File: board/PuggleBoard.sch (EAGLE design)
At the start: 130 parts, among them U1 LMP7704, U10 SN65LVDS2, U11 SN65LVDS1, U12 SN65LVDS1, U13 SN65LVDS1, U14 SN65MLVD201D, U15 24C, U2 ADS8331, U3 OPA4209, U4 AD5686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

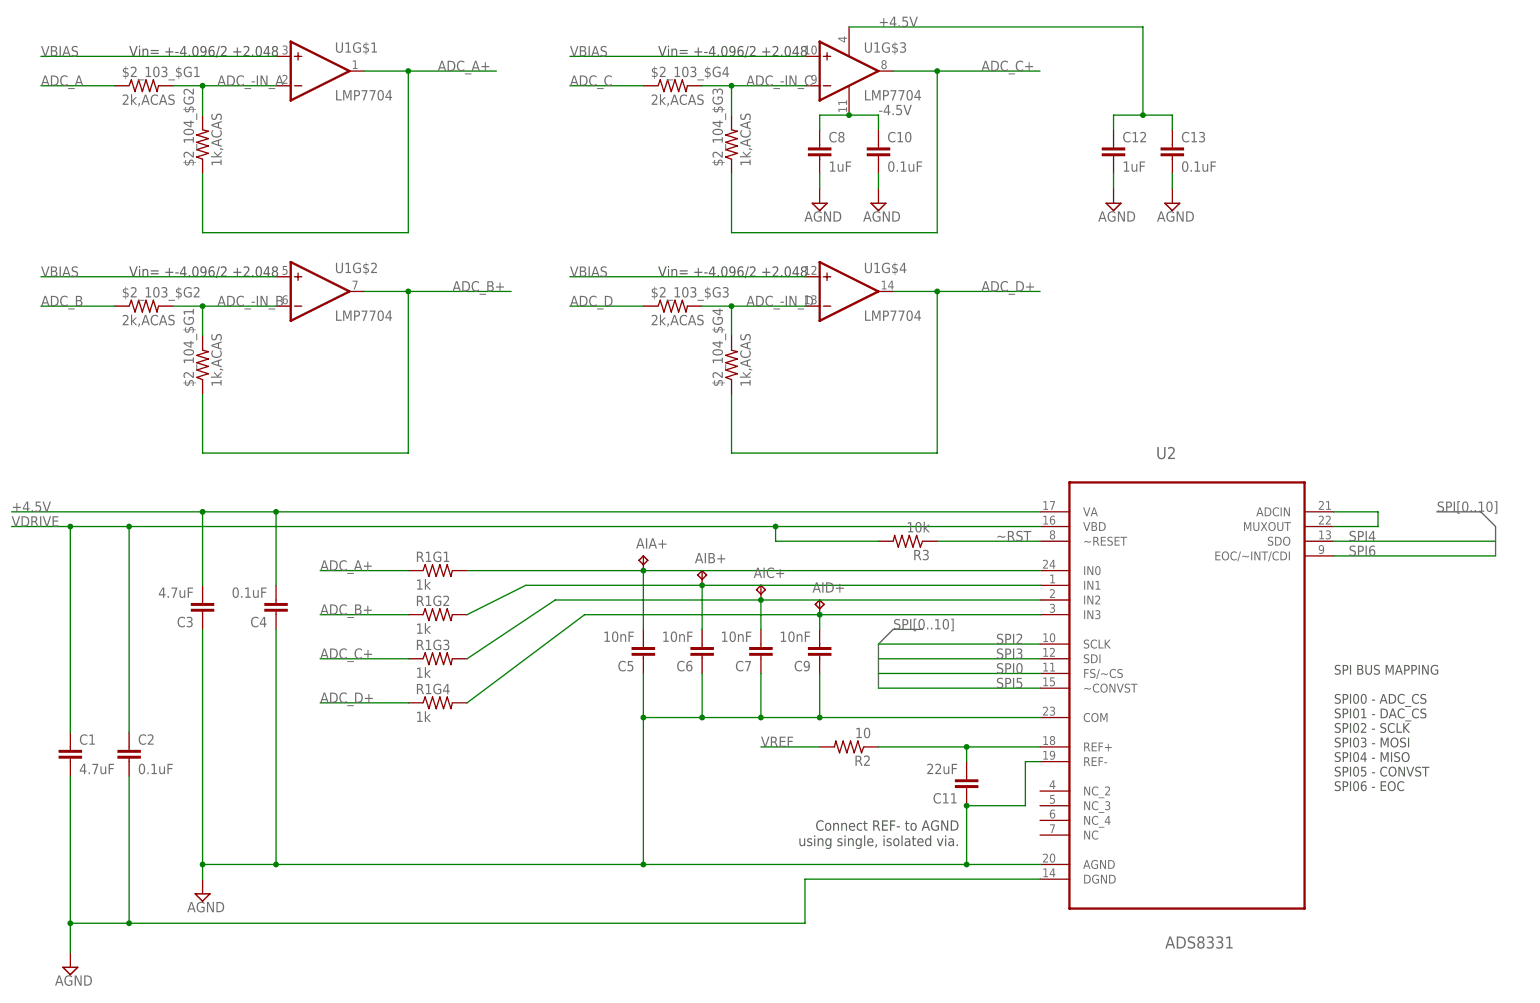
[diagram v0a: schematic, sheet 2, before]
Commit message: Nearly finished with layout. Need to get digital planes and LVDS signals routed. Hard parts done.
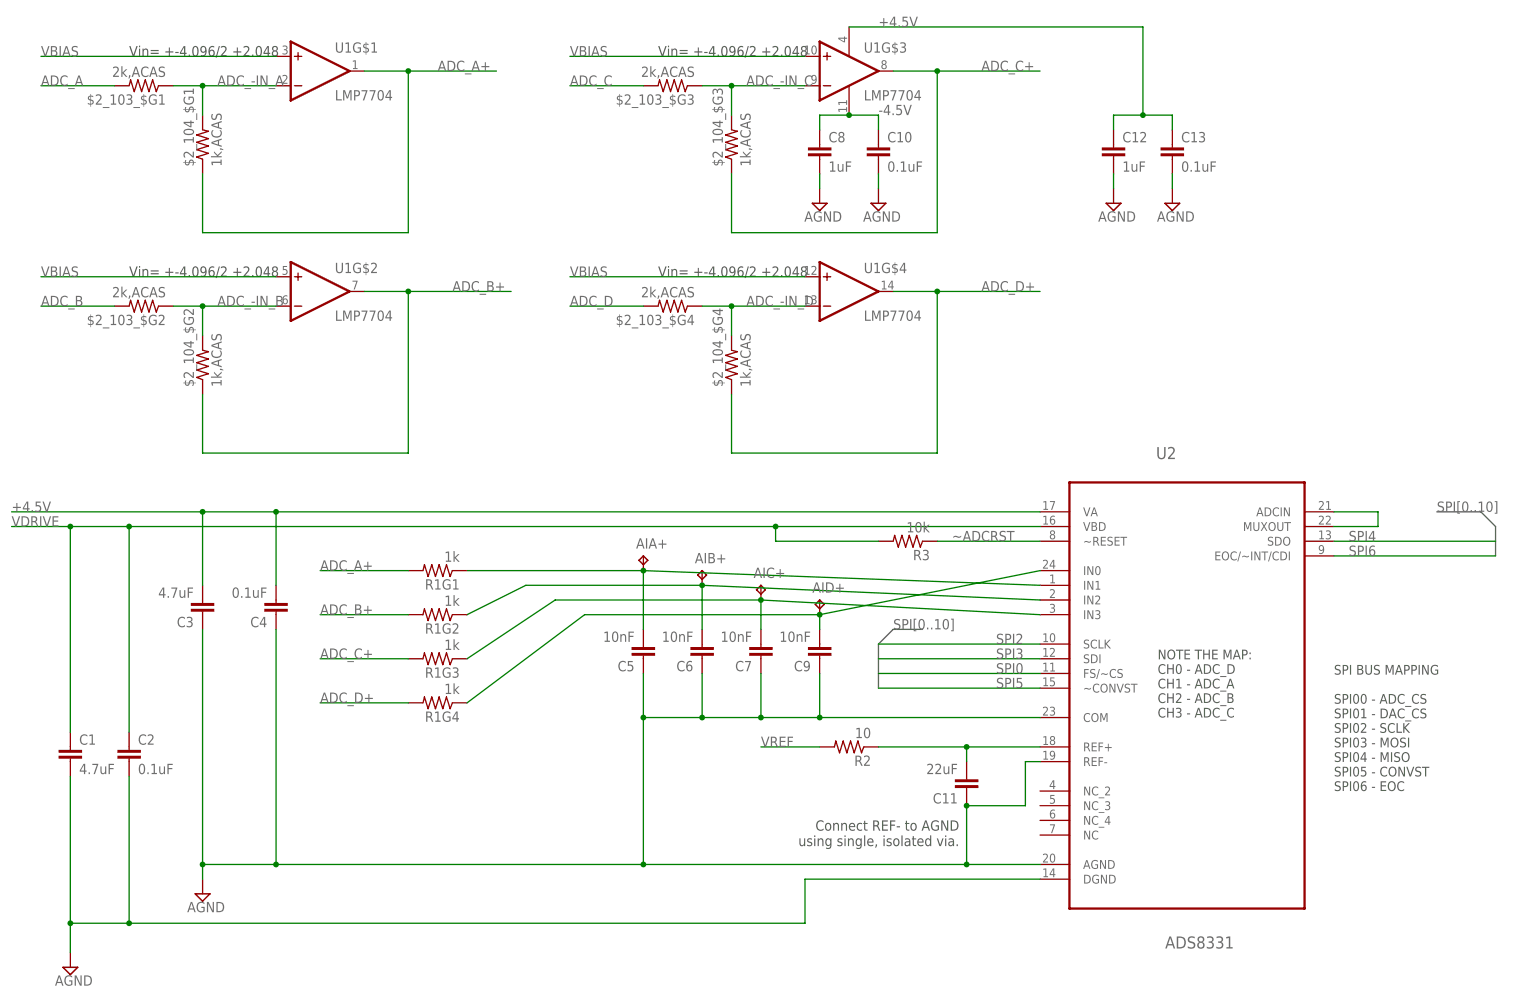
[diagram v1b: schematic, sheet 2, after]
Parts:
- C1, C3: device puggleboard:C_0805 -> puggleboard:C_0603
- C14: value 10uF -> 4.7uF; device puggleboard:C_0805 -> puggleboard:C_0603
- renumbered U$4 to SNYC
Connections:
- removed net AGND: R17.2
- removed net N$5: U9G$2.-IN, U9G$2.OUT
- removed net ~RST: R3.1, R5.1, U2.~RESET, U4.RESET*, U4.RSTSEL
- new net ~ADCRST: R3.1, U2.~RESET
- new net ~DACRST: R5.1, U4.RESET*, U4.RSTSEL
- net ADC_-IN_A: now also $2_103_$G1.1, $2_104_$G1.2; no longer $2_103_$G1.2, $2_104_$G2.2
- net ADC_-IN_B: now also $2_103_$G2.1, $2_104_$G2.2; no longer $2_103_$G2.2, $2_104_$G1.2
- net ADC_-IN_C: now also $2_103_$G3.1; no longer $2_103_$G4.2
- net ADC_-IN_D: now also $2_103_$G4.1; no longer $2_103_$G3.2
- net ADC_A: now also $2_103_$G1.2; no longer $2_103_$G1.1
- net ADC_A+: now also $2_104_$G1.1, R1G1.2; no longer $2_104_$G2.1, R1G1.1
- net ADC_B: now also $2_103_$G2.2; no longer $2_103_$G2.1
- net ADC_B+: now also $2_104_$G2.1, R1G2.2; no longer $2_104_$G1.1, R1G2.1
- net ADC_C: now also $2_103_$G3.2; no longer $2_103_$G4.1
- net ADC_C+: now also R1G3.2; no longer R1G3.1
- net ADC_D: now also $2_103_$G4.2; no longer $2_103_$G3.1
- net ADC_D+: now also R1G4.2; no longer R1G4.1
- net BOARD_TEMP: no longer BB1.AIN6
- net DAC_+IN_A: now also U4.VOUTD; no longer U4.VOUTA
- net DAC_+IN_B: now also U4.VOUTC; no longer U4.VOUTB
- net DAC_+IN_C: now also U4.VOUTA; no longer U4.VOUTC
- net DAC_+IN_D: now also U4.VOUTB; no longer U4.VOUTD
- net GND: now also R17.2
- net N$40: now also R1G1.1, U2.IN1; no longer R1G1.2, U2.IN0
- net N$41: now also R1G2.1, U2.IN2; no longer R1G2.2, U2.IN1
- net N$42: now also R1G3.1, U2.IN3; no longer R1G3.2, U2.IN2
- net N$43: now also R1G4.1, U2.IN0; no longer R1G4.2, U2.IN3
- net N$9: now also U9G$2.-IN, U9G$2.OUT
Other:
- note added: "NOTE THE MAP: CH0 - ADC_D CH1 - ADC_A CH2 - ADC_B CH3 - ADC_C"
- moved on the sheet: $2_103_$G1, $2_103_$G2, $2_103_$G3, $2_103_$G4, $2_104_$G1, $2_104_$G2, R1G1, R1G2, R1G3, R1G4

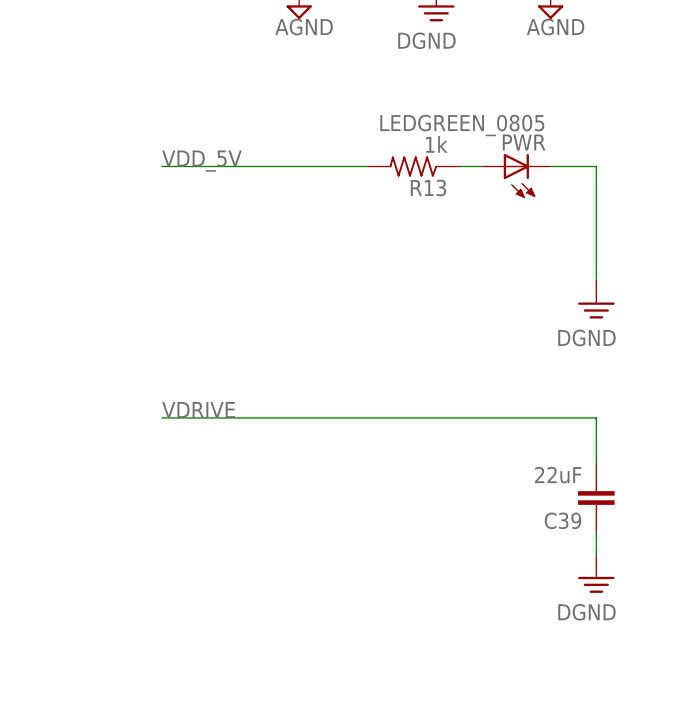
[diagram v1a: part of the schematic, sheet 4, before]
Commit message: Finished analog section. Digital section halfway done. Need revised pinout for sync signal from Yogi.
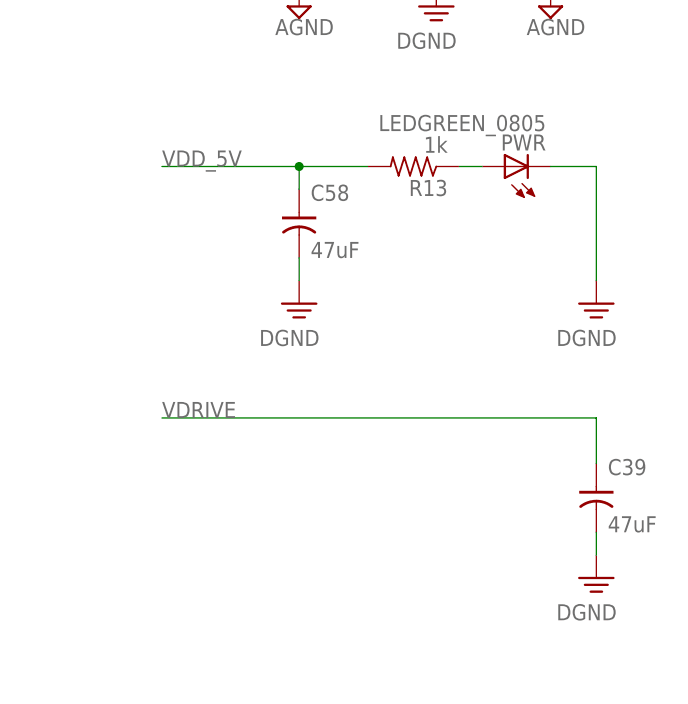
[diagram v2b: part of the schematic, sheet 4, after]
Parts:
- added C58: 47uF, puggleboard:C-POL_0807
- C39: value 22uF -> 47uF; device puggleboard:C_1206 -> puggleboard:C-POL_0807
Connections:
- new net PE: C58.-
- net GND: now also C39.-; no longer C39.1
- net VDD_5V: now also C58.+
- net VDRIVE: now also C39.+; no longer C39.2
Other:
- moved on the sheet: C39
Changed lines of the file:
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@@
 <part name="SUPPLY28" library="puggleboard" deviceset="DGND" device=""/>
 <part name="DGND11" library="puggleboard" deviceset="DGND" device="" value="DGND"/>
-<part name="C39" library="puggleboard" deviceset="C" device="_1206" value="22uF"/>
 <part name="FRAME2" library="puggleboard" deviceset="FRAME_A_L" device=""/>
 <part name="FRAME1" library="puggleboard" deviceset="FRAME_A_L" device=""/>
@@
 <part name="L3" library="puggleboard" deviceset="L" device="_0603" value="MPZ1608"/>
 <part name="L4" library="puggleboard" deviceset="L" device="_0603" value="MPZ1608"/>
+<part name="C39" library="puggleboard" deviceset="C-POL" device="_0807" value="47uF"/>
+<part name="C58" library="puggleboard" deviceset="C-POL" device="_0807" value="47uF"/>
+<part name="SUPPLY50" library="puggleboard" deviceset="DGND" device=""/>
 </parts>
 <sheets>
@@
 <instance part="SUPPLY47" gate="DGND" x="58.42" y="12.7"/>
 <instance part="DGND11" gate="DGND" x="152.4" y="-17.78"/>
-<instance part="C39" gate="C" x="152.4" y="-10.16" rot="R180"/>
 <instance part="FRAME4" gate="G$1" x="-109.22" y="-142.24"/>
 <instance part="FRAME4" gate="G$2" x="63.5" y="-142.24"/>
@@
 <instance part="L3" gate="L" x="53.34" y="-7.62" rot="R90"/>
 <instance part="L4" gate="L" x="53.34" y="-55.88" rot="R90"/>
+<instance part="C39" gate="C" x="152.4" y="-10.16"/>
+<instance part="C58" gate="C" x="119.38" y="20.32"/>
+<instance part="SUPPLY50" gate="DGND" x="119.38" y="12.7"/>
 </instances>
 <busses>
@@
 <pinref part="R13" gate="R" pin="2"/>
 <label x="104.14" y="27.94" size="1.778" layer="95"/>
-<wire x1="127" y1="27.94" x2="104.14" y2="27.94" width="0.1524" layer="91"/>
+<wire x1="127" y1="27.94" x2="119.38" y2="27.94" width="0.1524" layer="91"/>
+<pinref part="C58" gate="C" pin="+"/>
+<wire x1="119.38" y1="27.94" x2="104.14" y2="27.94" width="0.1524" layer="91"/>
+<wire x1="119.38" y1="25.4" x2="119.38" y2="27.94" width="0.1524" layer="91"/>
+<junction x="119.38" y="27.94"/>
 </segment>
 <segment>
@@
 </segment>
 <segment>
-<pinref part="C39" gate="C" pin="1"/>
 <pinref part="DGND11" gate="DGND" pin="PE"/>
 <wire x1="152.4" y1="-12.7" x2="152.4" y2="-15.24" width="0.1524" layer="91"/>
+<pinref part="C39" gate="C" pin="-"/>
 </segment>
 <segment>
@@
 <net name="VDRIVE" class="0">
 <segment>
-<pinref part="C39" gate="C" pin="2"/>
 <wire x1="104.14" y1="0" x2="152.4" y2="0" width="0.1524" layer="91"/>
 <wire x1="152.4" y1="-5.08" x2="152.4" y2="0" width="0.1524" layer="91"/>
 <label x="104.14" y="0" size="1.778" layer="95"/>
+<pinref part="C39" gate="C" pin="+"/>
 </segment>
 </net>
@@
 </segment>
 </net>
+<net name="PE" class="0">
+<segment>
+<pinref part="SUPPLY50" gate="DGND" pin="PE"/>
+<pinref part="C58" gate="C" pin="-"/>
+<wire x1="119.38" y1="15.24" x2="119.38" y2="17.78" width="0.1524" layer="91"/>
+</segment>
+</net>

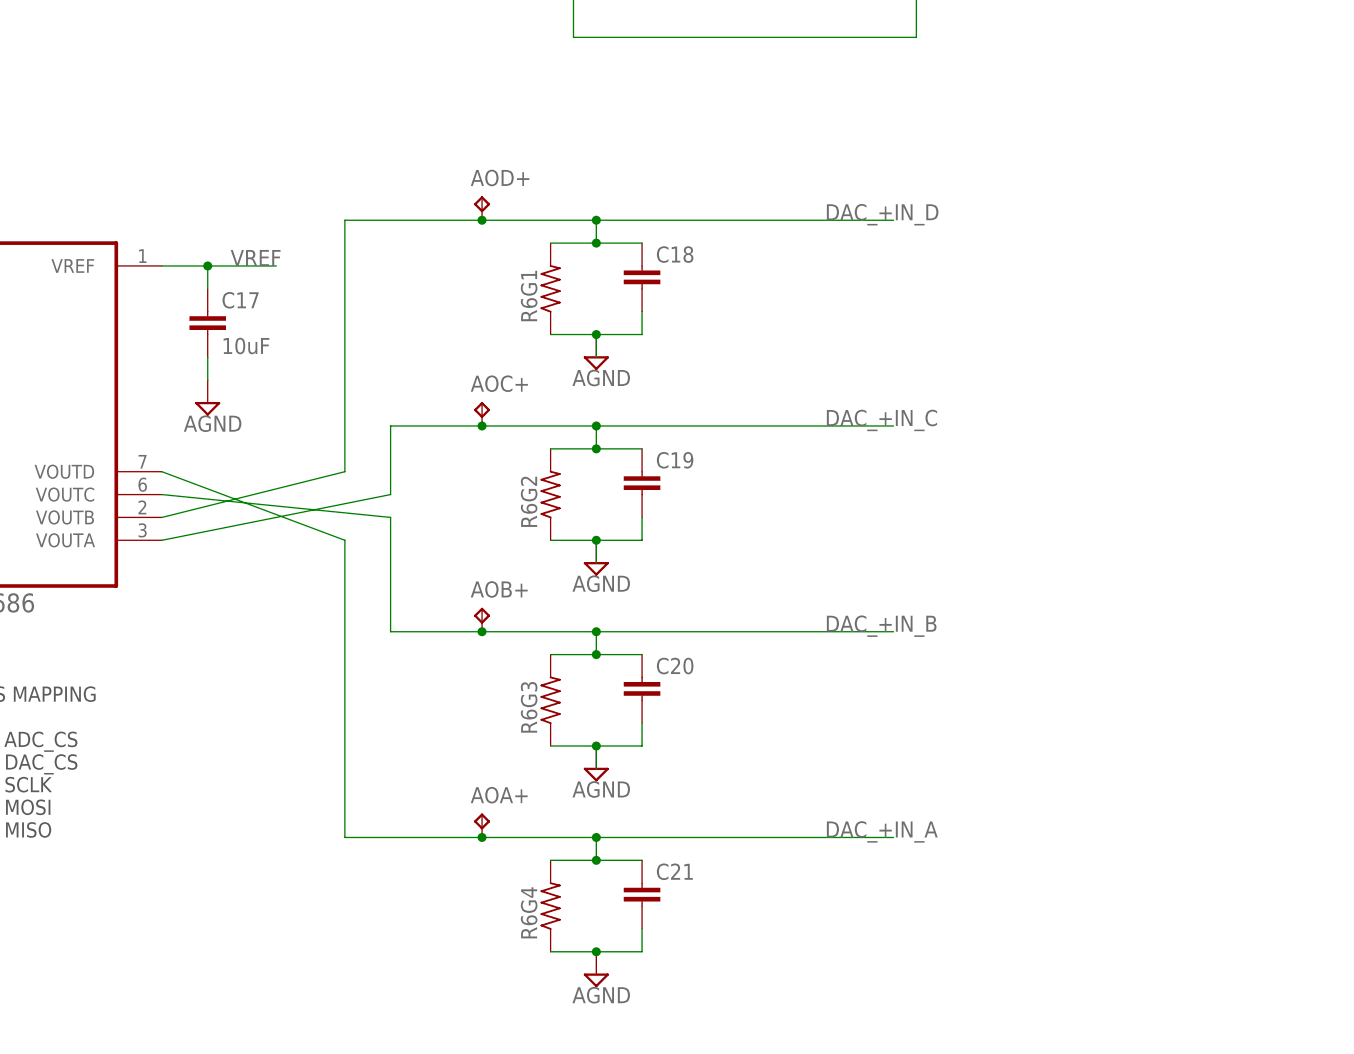
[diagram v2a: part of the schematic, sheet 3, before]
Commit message: Minor schematic cleanup.
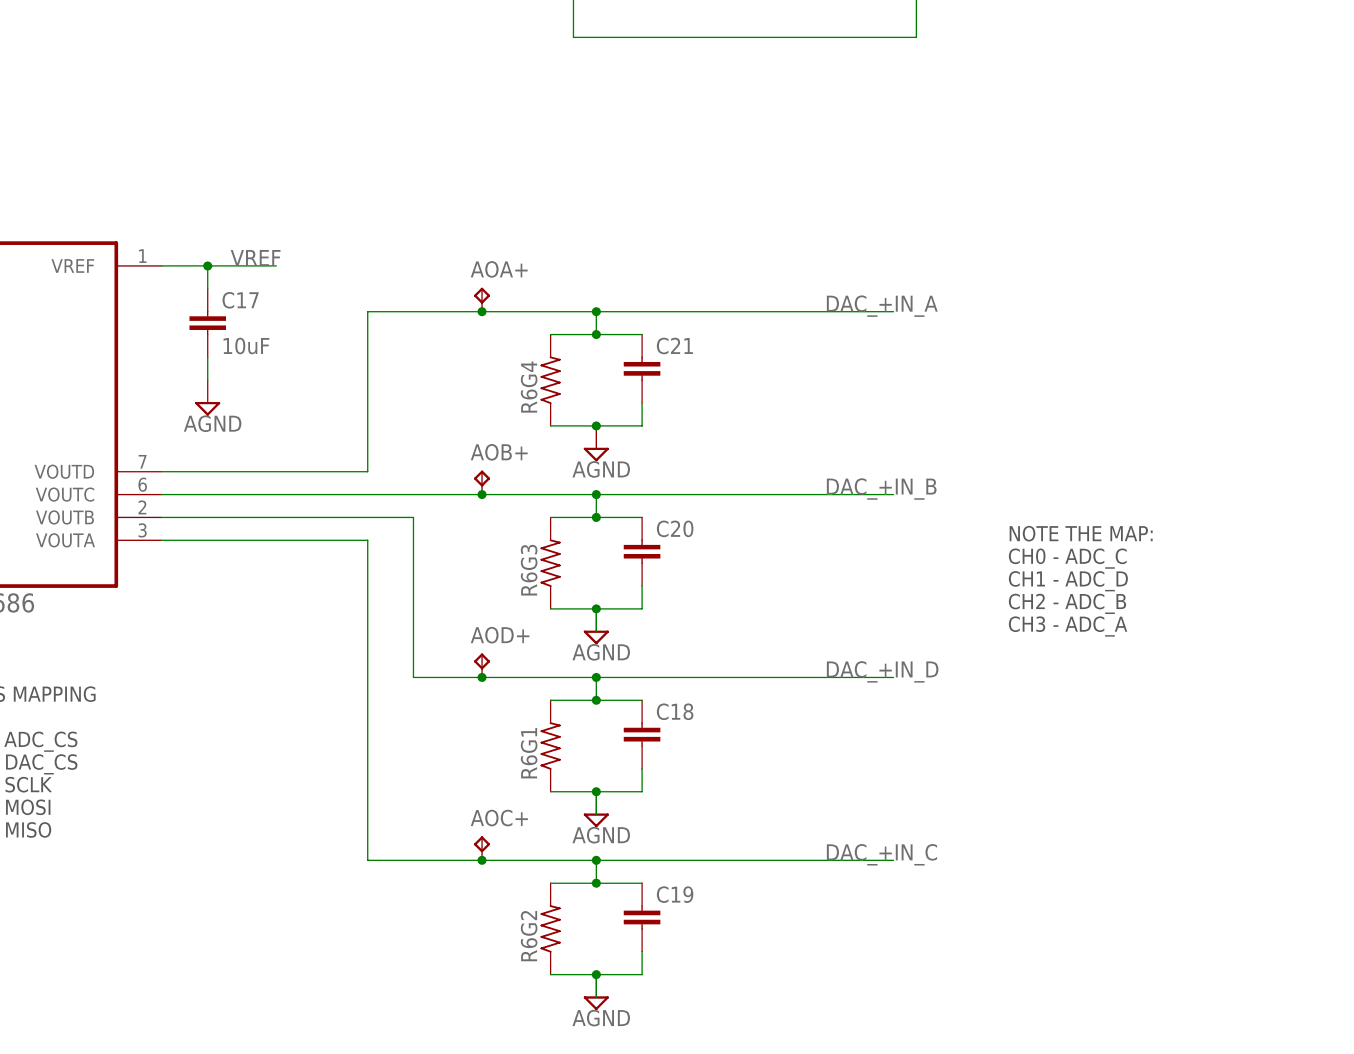
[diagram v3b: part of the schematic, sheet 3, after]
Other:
- note added: "NOTE THE MAP: CH0 - ADC_C CH1 - ADC_D CH2 - ADC_B CH3 - ADC_A"
- moved on the sheet: AIA+, AIB+, AIC+, AID+, AOA+, AOB+, AOC+, AOD+, C18, C19, C20, C21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

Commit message: Fixed a few DRC errors.
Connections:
- removed net PE: C58.-
- net GND: now also C58.-
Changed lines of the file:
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@@
 <pinref part="SUPPLY49" gate="G$1" pin="AGND"/>
+</segment>
+<segment>
+<pinref part="SUPPLY50" gate="DGND" pin="PE"/>
+<pinref part="C58" gate="C" pin="-"/>
+<wire x1="119.38" y1="15.24" x2="119.38" y2="17.78" width="0.1524" layer="91"/>
 </segment>
 </net>
@@
 </segment>
 </net>
-<net name="PE" class="0">
-<segment>
-<pinref part="SUPPLY50" gate="DGND" pin="PE"/>
-<pinref part="C58" gate="C" pin="-"/>
-<wire x1="119.38" y1="15.24" x2="119.38" y2="17.78" width="0.1524" layer="91"/>
-</segment>
-</net>
